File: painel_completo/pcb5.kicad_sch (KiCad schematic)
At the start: 17 parts, among them J1 Conn_02x05_Odd_Even, J13 Conn_02x02_Odd_Even, J15 Conn_02x10_Odd_Even, SW13 SW_Push_LED, SW14 SW_Push_LED, SW15 SW_Push_LED, SW16 SW_Push_LED, SW17 SW_Push_LED, SW18 SW_Push_LED

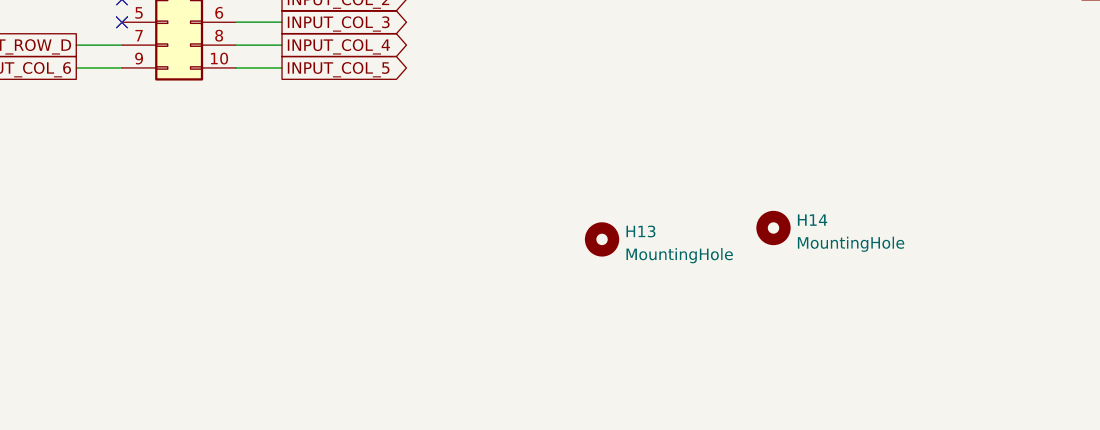
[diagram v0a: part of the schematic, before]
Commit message: adição furos fixação e alteração máscara de componentes
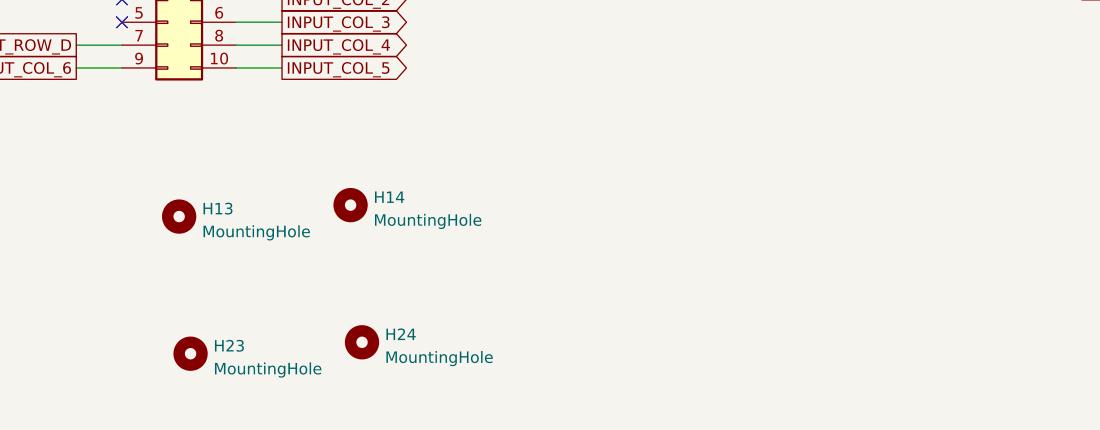
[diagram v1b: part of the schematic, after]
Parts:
- added H23, H24: MountingHole, MountingHole:MountingHole_3.2mm_M3, symbol Mechanical:MountingHole
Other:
- moved on the sheet: H13, H14
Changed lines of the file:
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@@
     (pin "4")
+  )
+  (symbol (lib_id "Mechanical:MountingHole") (at 132.08 173.99 0) (unit 1)
+    (in_bom yes) (on_board yes) (fields_autoplaced)
+    (property "Reference" "H24" (id 0) (at 134.62 173.1553 0)
+      (effects (font (size 1.27 1.27)) (justify left))
+    )
+    (property "Value" "MountingHole" (id 1) (at 134.62 175.6922 0)
+      (effects (font (size 1.27 1.27)) (justify left))
+    )
+    (property "Footprint" "MountingHole:MountingHole_3.2mm_M3" (id 2) (at 132.08 173.99 0)
+      (effects (font (size 1.27 1.27)) hide)
+    )
+    (property "Datasheet" "~" (id 3) (at 132.08 173.99 0)
+      (effects (font (size 1.27 1.27)) hide)
+    )
   )
   (symbol (lib_id "Connector_Generic:Conn_02x10_Odd_Even") (at 57.15 167.64 0) (unit 1)
@@
     (pin "9")
   )
+  (symbol (lib_id "Mechanical:MountingHole") (at 113.03 175.26 0) (unit 1)
+    (in_bom yes) (on_board yes) (fields_autoplaced)
+    (property "Reference" "H23" (id 0) (at 115.57 174.4253 0)
+      (effects (font (size 1.27 1.27)) (justify left))
+    )
+    (property "Value" "MountingHole" (id 1) (at 115.57 176.9622 0)
+      (effects (font (size 1.27 1.27)) (justify left))
+    )
+    (property "Footprint" "MountingHole:MountingHole_3.2mm_M3" (id 2) (at 113.03 175.26 0)
+      (effects (font (size 1.27 1.27)) hide)
+    )
+    (property "Datasheet" "~" (id 3) (at 113.03 175.26 0)
+      (effects (font (size 1.27 1.27)) hide)
+    )
+  )
   (symbol (lib_id "Device:D_Small") (at 245.11 63.5 180) (unit 1)
     (in_bom yes) (on_board yes) (fields_autoplaced)
@@
     (pin "2")
   )
-  (symbol (lib_id "Mechanical:MountingHole") (at 177.8 161.29 0) (unit 1)
+  (symbol (lib_id "Mechanical:MountingHole") (at 130.81 158.75 0) (unit 1)
     (in_bom yes) (on_board yes) (fields_autoplaced)
-    (property "Reference" "H14" (id 0) (at 180.34 160.4553 0)
+    (property "Reference" "H14" (id 0) (at 133.35 157.9153 0)
       (effects (font (size 1.27 1.27)) (justify left))
     )
-    (property "Value" "MountingHole" (id 1) (at 180.34 162.9922 0)
+    (property "Value" "MountingHole" (id 1) (at 133.35 160.4522 0)
       (effects (font (size 1.27 1.27)) (justify left))
     )
-    (property "Footprint" "MountingHole:MountingHole_3.2mm_M3" (id 2) (at 177.8 161.29 0)
+    (property "Footprint" "MountingHole:MountingHole_3.2mm_M3" (id 2) (at 130.81 158.75 0)
       (effects (font (size 1.27 1.27)) hide)
     )
-    (property "Datasheet" "~" (id 3) (at 177.8 161.29 0)
+    (property "Datasheet" "~" (id 3) (at 130.81 158.75 0)
       (effects (font (size 1.27 1.27)) hide)
     )
@@
     (pin "4")
   )
-  (symbol (lib_id "Mechanical:MountingHole") (at 158.75 162.56 0) (unit 1)
+  (symbol (lib_id "Mechanical:MountingHole") (at 111.76 160.02 0) (unit 1)
     (in_bom yes) (on_board yes) (fields_autoplaced)
-    (property "Reference" "H13" (id 0) (at 161.29 161.7253 0)
+    (property "Reference" "H13" (id 0) (at 114.3 159.1853 0)
       (effects (font (size 1.27 1.27)) (justify left))
     )
-    (property "Value" "MountingHole" (id 1) (at 161.29 164.2622 0)
+    (property "Value" "MountingHole" (id 1) (at 114.3 161.7222 0)
       (effects (font (size 1.27 1.27)) (justify left))
     )
-    (property "Footprint" "MountingHole:MountingHole_3.2mm_M3" (id 2) (at 158.75 162.56 0)
+    (property "Footprint" "MountingHole:MountingHole_3.2mm_M3" (id 2) (at 111.76 160.02 0)
       (effects (font (size 1.27 1.27)) hide)
     )
-    (property "Datasheet" "~" (id 3) (at 158.75 162.56 0)
+    (property "Datasheet" "~" (id 3) (at 111.76 160.02 0)
       (effects (font (size 1.27 1.27)) hide)
     )
